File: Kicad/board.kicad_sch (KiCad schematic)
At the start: 32 parts, among them SW1 SW_Push, SW10 SW_Push, SW11 SW_Push, SW12 SW_Push, SW13 RotaryEncoder, SW2 SW_Push, SW3 SW_Push, SW4 SW_Push, SW5 SW_Push, SW6 SW_Push, SW7 SW_Push, SW8 SW_Push, SW9 SW_Push, U1 XIAO-ESP32-S3-DIP, U2 KY-023, U3 KY-023

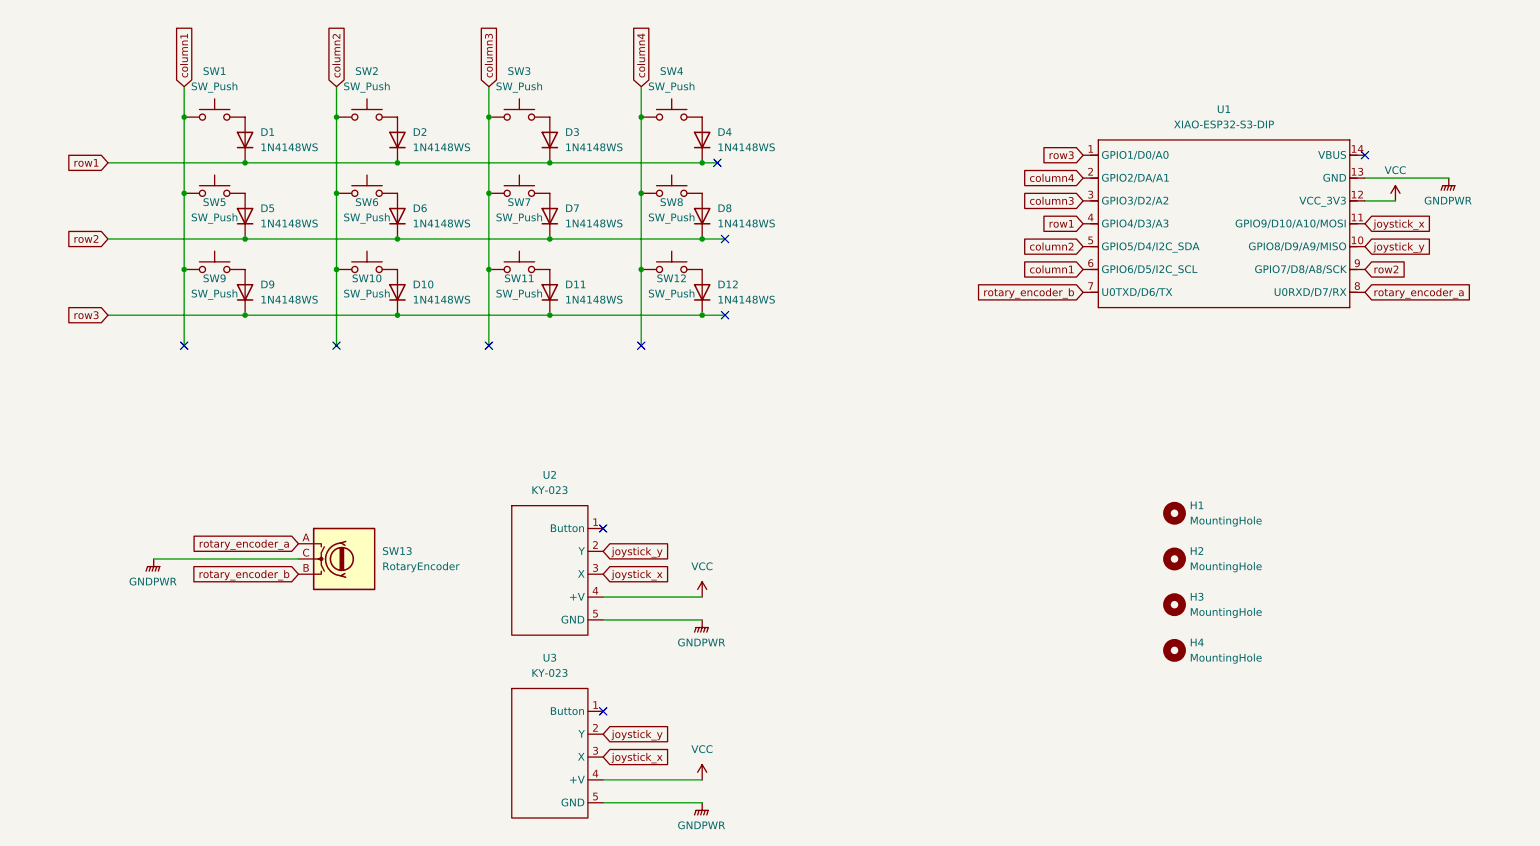
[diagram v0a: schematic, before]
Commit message: [add] add an oled device and revise pin assign
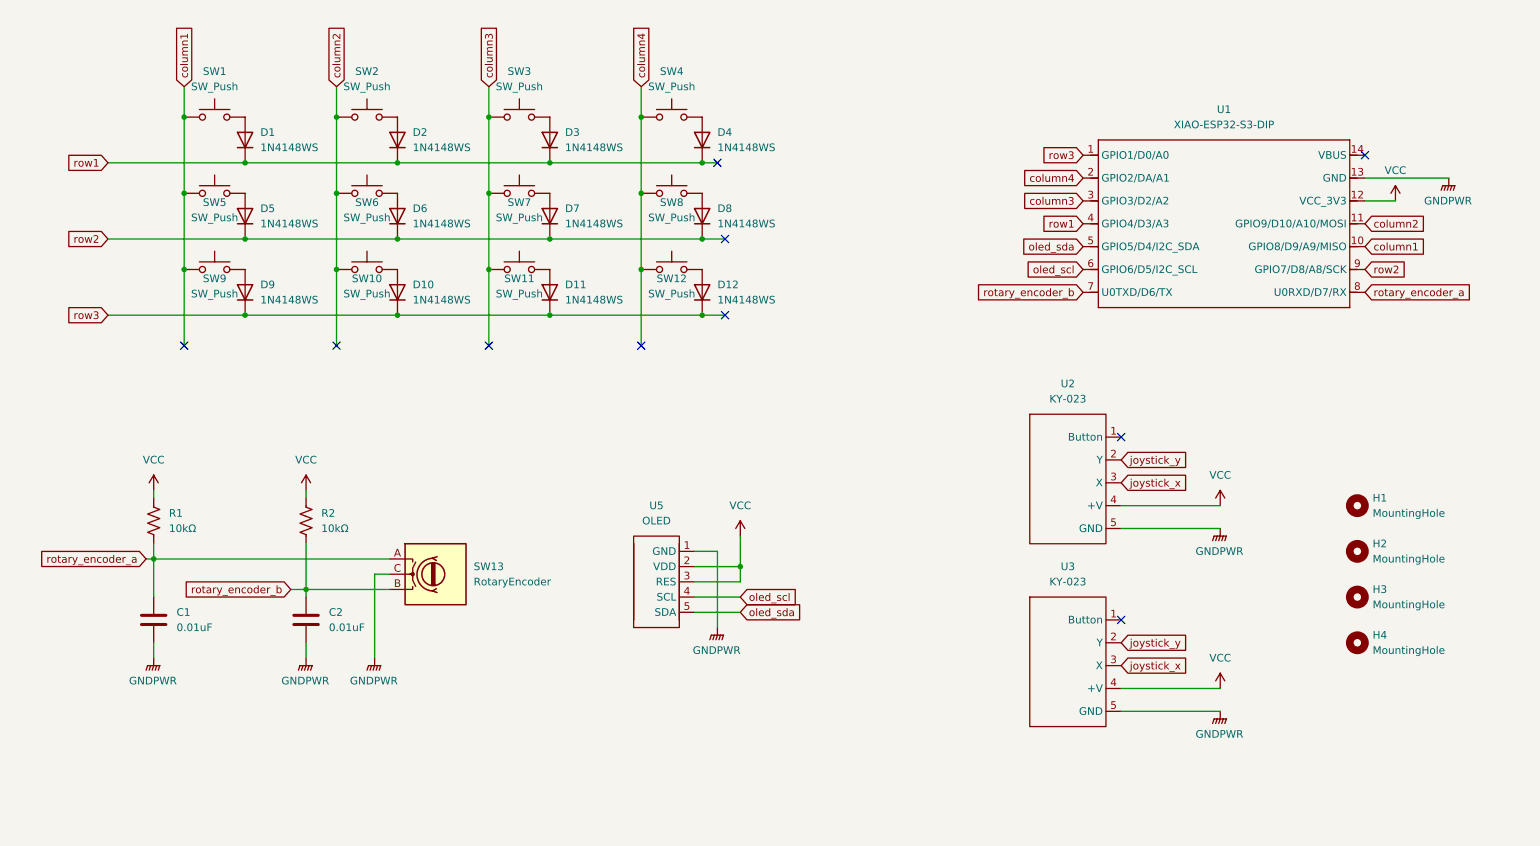
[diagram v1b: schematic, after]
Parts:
- added C1, C2: 0.01uF, symbol Device:C
- added R1, R2: 10kΩ, symbol Device:R_US
- added U5: OLED, symbol my_parts:oled
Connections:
- net GNDPWR: now also C1.2, C2.2, U5.1 (GND)
- net VCC: now also R1.1, R2.1, U5.2 (VDD), U5.3 (RES)
- net column1: now also U1.10 (GPIO8/D9/A9/MISO); no longer U1.6 (GPIO6/D5/I2C_SCL)
- net column2: now also U1.11 (GPIO9/D10/A10/MOSI); no longer U1.5 (GPIO5/D4/I2C_SDA)
- net joystick_x: no longer U1.11 (GPIO9/D10/A10/MOSI)
- net joystick_y: no longer U1.10 (GPIO8/D9/A9/MISO)
- net rotary_encoder_a: now also C1.1, R1.2
- net rotary_encoder_b: now also C2.1, R2.2
- new net oled_scl: U1.6 (GPIO6/D5/I2C_SCL), U5.4 (SCL)
- new net oled_sda: U1.5 (GPIO5/D4/I2C_SDA), U5.5 (SDA)
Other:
- moved on the sheet: H1, H2, H3, H4, SW13, U2, U3

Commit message: [update] update footprint
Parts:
- C1, C2: footprint (none) -> Capacitor_SMD:C_0805_2012Metric_Pad1.18x1.45mm_HandSolder
- D1, D10, D11, D12, D2, D3, D4, D5, D6, D7, D8, D9: value 1N4148WS -> 1N4148W; footprint mylib:1n4148ws_reversible -> Diode_THT:D_DO-35_SOD27_P7.62mm_Horizontal
- R1, R2: footprint (none) -> Resistor_THT:R_Axial_DIN0207_L6.3mm_D2.5mm_P10.16mm_Horizontal
- U2: now left out of the parts list
- U4: renamed from U3; now left out of the parts list
- renumbered U5 to U3
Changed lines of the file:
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@@
 			)
 		)
-		(property "Footprint" ""
+		(property "Footprint" "Resistor_THT:R_Axial_DIN0207_L6.3mm_D2.5mm_P10.16mm_Horizontal"
 			(at 68.326 118.364 90)
 			(effects
@@
 		(unit 1)
 		(exclude_from_sim no)
-		(in_bom yes)
-		(on_board yes)
+		(in_bom no)
+		(on_board no)
 		(dnp no)
 		(fields_autoplaced yes)
-		(property "Reference" "U3"
+		(property "Reference" "U4"
 			(at 194.31 125.73 0)
 			(effects
@@
 			(project "board"
 				(path "/e49ea350-db18-4e55-8e96-c45c407ec11d"
-					(reference "U3")
+					(reference "U4")
 					(unit 1)
 				)
@@
 			)
 		)
-		(property "Value" "1N4148WS"
+		(property "Value" "1N4148W"
 			(at 110.49 55.8799 90)
 			(effects
@@
 			)
 		)
-		(property "Footprint" "mylib:1n4148ws_reversible"
+		(property "Footprint" "Diode_THT:D_DO-35_SOD27_P7.62mm_Horizontal"
 			(at 112.395 54.61 0)
 			(effects
@@
 			)
 		)
-		(property "Value" "1N4148WS"
+		(property "Value" "1N4148W"
 			(at 135.89 55.8799 90)
 			(effects
@@
 			)
 		)
-		(property "Footprint" "mylib:1n4148ws_reversible"
+		(property "Footprint" "Diode_THT:D_DO-35_SOD27_P7.62mm_Horizontal"
 			(at 137.795 54.61 0)
 			(effects
@@
 		(dnp no)
 		(fields_autoplaced yes)
-		(property "Reference" "U5"
+		(property "Reference" "U3"
 			(at 125.73 115.57 0)
 			(effects
@@
 			(project ""
 				(path "/e49ea350-db18-4e55-8e96-c45c407ec11d"
-					(reference "U5")
+					(reference "U3")
 					(unit 1)
 				)
@@
 			)
 		)
-		(property "Value" "1N4148WS"
+		(property "Value" "1N4148W"
 			(at 135.89 81.2799 90)
 			(effects
@@
 			)
 		)
-		(property "Footprint" "mylib:1n4148ws_reversible"
+		(property "Footprint" "Diode_THT:D_DO-35_SOD27_P7.62mm_Horizontal"
 			(at 137.795 80.01 0)
 			(effects
@@
 			)
 		)
-		(property "Footprint" ""
+		(property "Footprint" "Capacitor_SMD:C_0805_2012Metric_Pad1.18x1.45mm_HandSolder"
 			(at 42.8752 138.43 0)
 			(effects
@@
 		(dnp no)
 		(fields_autoplaced yes)
-		(property "Reference" "#PWR07"
+		(property "Reference" "#PWR013"
 			(at 219.71 154.94 0)
 			(effects
@@
 			(project "board"
 				(path "/e49ea350-db18-4e55-8e96-c45c407ec11d"
-					(reference "#PWR07")
+					(reference "#PWR013")
 					(unit 1)
 				)
@@
 			)
 		)
-		(property "Value" "1N4148WS"
+		(property "Value" "1N4148W"
 			(at 85.09 68.5799 90)
 			(effects
@@
 			)
 		)
-		(property "Footprint" "mylib:1n4148ws_reversible"
+		(property "Footprint" "Diode_THT:D_DO-35_SOD27_P7.62mm_Horizontal"
 			(at 86.995 67.31 0)
 			(effects
@@
 			)
 		)
-		(property "Value" "1N4148WS"
+		(property "Value" "1N4148W"
 			(at 59.69 81.2799 90)
 			(effects
@@
 			)
 		)
-		(property "Footprint" "mylib:1n4148ws_reversible"
+		(property "Footprint" "Diode_THT:D_DO-35_SOD27_P7.62mm_Horizontal"
 			(at 61.595 80.01 0)
 			(effects
@@
 		(unit 1)
 		(exclude_from_sim no)
-		(in_bom yes)
-		(on_board yes)
+		(in_bom no)
+		(on_board no)
 		(dnp no)
 		(fields_autoplaced yes)
@@
 		(dnp no)
 		(fields_autoplaced yes)
-		(property "Reference" "#PWR012"
+		(property "Reference" "#PWR07"
 			(at 139.7 124.46 0)
 			(effects
@@
 			(project ""
 				(path "/e49ea350-db18-4e55-8e96-c45c407ec11d"
-					(reference "#PWR012")
+					(reference "#PWR07")
 					(unit 1)
 				)
@@
 			)
 		)
-		(property "Value" "1N4148WS"
+		(property "Value" "1N4148W"
 			(at 85.09 81.2799 90)
 			(effects
@@
 			)
 		)
-		(property "Footprint" "mylib:1n4148ws_reversible"
+		(property "Footprint" "Diode_THT:D_DO-35_SOD27_P7.62mm_Horizontal"
 			(at 86.995 80.01 0)
 			(effects
@@
 		(dnp no)
 		(fields_autoplaced yes)
-		(property "Reference" "#PWR06"
+		(property "Reference" "#PWR012"
 			(at 219.71 149.86 0)
 			(effects
@@
 			(project "board"
 				(path "/e49ea350-db18-4e55-8e96-c45c407ec11d"
-					(reference "#PWR06")
+					(reference "#PWR012")
 					(unit 1)
 				)
@@
 		(dnp no)
 		(fields_autoplaced yes)
-		(property "Reference" "#PWR09"
+		(property "Reference" "#PWR04"
 			(at 67.31 116.84 0)
 			(effects
@@
 			(project "board"
 				(path "/e49ea350-db18-4e55-8e96-c45c407ec11d"
-					(reference "#PWR09")
+					(reference "#PWR04")
 					(unit 1)
 				)
@@
 			)
 		)
-		(property "Value" "1N4148WS"
+		(property "Value" "1N4148W"
 			(at 135.89 68.5799 90)
 			(effects
@@
 			)
 		)
-		(property "Footprint" "mylib:1n4148ws_reversible"
+		(property "Footprint" "Diode_THT:D_DO-35_SOD27_P7.62mm_Horizontal"
 			(at 137.795 67.31 0)
 			(effects
@@
 			)
 		)
-		(property "Value" "1N4148WS"
+		(property "Value" "1N4148W"
 			(at 110.49 81.2799 90)
 			(effects
@@
 			)
 		)
-		(property "Footprint" "mylib:1n4148ws_reversible"
+		(property "Footprint" "Diode_THT:D_DO-35_SOD27_P7.62mm_Horizontal"
 			(at 112.395 80.01 0)
 			(effects
@@
 		(dnp no)
 		(fields_autoplaced yes)
-		(property "Reference" "#PWR013"
+		(property "Reference" "#PWR08"
 			(at 135.89 140.97 0)
 			(effects
@@
 			(project ""
 				(path "/e49ea350-db18-4e55-8e96-c45c407ec11d"
-					(reference "#PWR013")
+					(reference "#PWR08")
 					(unit 1)
 				)
@@
 		(dnp no)
 		(fields_autoplaced yes)
-		(property "Reference" "#PWR05"
+		(property "Reference" "#PWR06"
 			(at 219.71 124.46 0)
 			(effects
@@
 			(project ""
 				(path "/e49ea350-db18-4e55-8e96-c45c407ec11d"
-					(reference "#PWR05")
+					(reference "#PWR06")
 					(unit 1)
 				)
@@
 			)
 		)
-		(property "Footprint" ""
+		(property "Footprint" "Capacitor_SMD:C_0805_2012Metric_Pad1.18x1.45mm_HandSolder"
 			(at 68.2752 138.43 0)
 			(effects
@@
 			)
 		)
-		(property "Value" "1N4148WS"
+		(property "Value" "1N4148W"
 			(at 59.69 68.5799 90)
 			(effects
@@
 			)
 		)
-		(property "Footprint" "mylib:1n4148ws_reversible"
+		(property "Footprint" "Diode_THT:D_DO-35_SOD27_P7.62mm_Horizontal"
 			(at 61.595 67.31 0)
 			(effects
@@
 		(dnp no)
 		(fields_autoplaced yes)
-		(property "Reference" "#PWR011"
+		(property "Reference" "#PWR010"
 			(at 67.31 146.05 0)
 			(effects
@@
 			(project "board"
 				(path "/e49ea350-db18-4e55-8e96-c45c407ec11d"
-					(reference "#PWR011")
+					(reference "#PWR010")
 					(unit 1)
 				)
@@
 		(dnp no)
 		(fields_autoplaced yes)
-		(property "Reference" "#PWR03"
+		(property "Reference" "#PWR011"
 			(at 78.74 146.05 0)
 			(effects
@@
 			(project ""
 				(path "/e49ea350-db18-4e55-8e96-c45c407ec11d"
-					(reference "#PWR03")
+					(reference "#PWR011")
 					(unit 1)
 				)
@@
 		(dnp no)
 		(fields_autoplaced yes)
-		(property "Reference" "#PWR04"
+		(property "Reference" "#PWR05"
 			(at 219.71 119.38 0)
 			(effects
@@
 			(project ""
 				(path "/e49ea350-db18-4e55-8e96-c45c407ec11d"
-					(reference "#PWR04")
+					(reference "#PWR05")
 					(unit 1)
 				)
@@
 			)
 		)
-		(property "Value" "1N4148WS"
+		(property "Value" "1N4148W"
 			(at 85.09 55.8799 90)
 			(effects
@@
 			)
 		)
-		(property "Footprint" "mylib:1n4148ws_reversible"
+		(property "Footprint" "Diode_THT:D_DO-35_SOD27_P7.62mm_Horizontal"
 			(at 86.995 54.61 0)
 			(effects
@@
 			)
 		)
-		(property "Footprint" ""
+		(property "Footprint" "Resistor_THT:R_Axial_DIN0207_L6.3mm_D2.5mm_P10.16mm_Horizontal"
 			(at 42.926 118.364 90)
 			(effects
@@
 			)
 		)
-		(property "Value" "1N4148WS"
+		(property "Value" "1N4148W"
 			(at 110.49 68.5799 90)
 			(effects
@@
 			)
 		)
-		(property "Footprint" "mylib:1n4148ws_reversible"
+		(property "Footprint" "Diode_THT:D_DO-35_SOD27_P7.62mm_Horizontal"
 			(at 112.395 67.31 0)
 			(effects
@@
 			)
 		)
-		(property "Value" "1N4148WS"
+		(property "Value" "1N4148W"
 			(at 59.69 55.8799 90)
 			(effects
@@
 			)
 		)
-		(property "Footprint" "mylib:1n4148ws_reversible"
+		(property "Footprint" "Diode_THT:D_DO-35_SOD27_P7.62mm_Horizontal"
 			(at 61.595 54.61 0)
 			(effects
@@
 		(dnp no)
 		(fields_autoplaced yes)
-		(property "Reference" "#PWR010"
+		(property "Reference" "#PWR09"
 			(at 41.91 146.05 0)
 			(effects
@@
 			(project "board"
 				(path "/e49ea350-db18-4e55-8e96-c45c407ec11d"
-					(reference "#PWR010")
+					(reference "#PWR09")
 					(unit 1)
 				)
@@
 		(dnp no)
 		(fields_autoplaced yes)
-		(property "Reference" "#PWR08"
+		(property "Reference" "#PWR03"
 			(at 41.91 116.84 0)
 			(effects
@@
 			(project ""
 				(path "/e49ea350-db18-4e55-8e96-c45c407ec11d"
-					(reference "#PWR08")
+					(reference "#PWR03")
 					(unit 1)
 				)

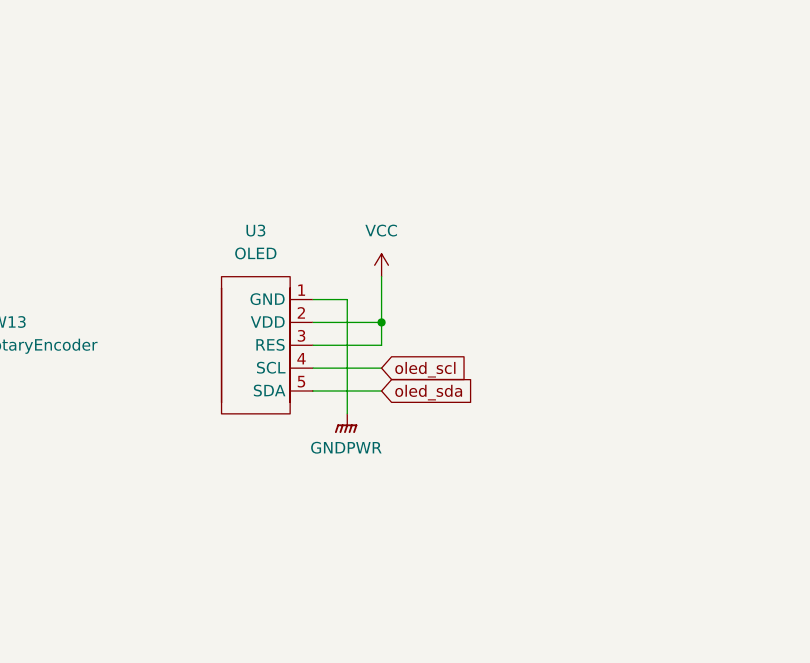
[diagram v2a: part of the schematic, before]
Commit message: [add] add solder jumpers to support reversible pin holes
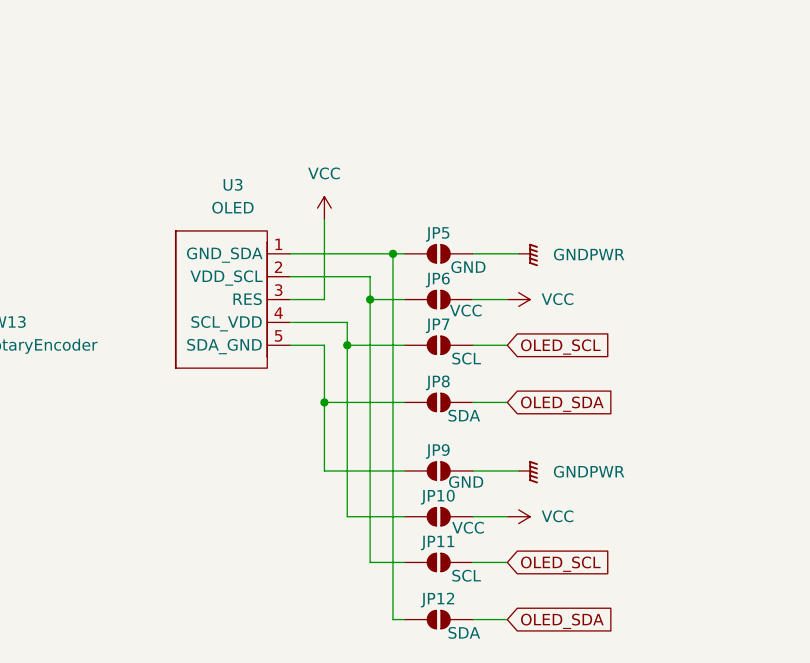
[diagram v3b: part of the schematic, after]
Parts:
- added JP10, JP6: VCC, Jumper:SolderJumper-2_P1.3mm_Open_TrianglePad1.0x1.5mm, symbol Jumper:SolderJumper_2_Open
- added JP11, JP7: SCL, Jumper:SolderJumper-2_P1.3mm_Open_TrianglePad1.0x1.5mm, symbol Jumper:SolderJumper_2_Open
- added JP12, JP8: SDA, Jumper:SolderJumper-2_P1.3mm_Open_TrianglePad1.0x1.5mm, symbol Jumper:SolderJumper_2_Open
- added JP5, JP9: GND, Jumper:SolderJumper-2_P1.3mm_Open_TrianglePad1.0x1.5mm, symbol Jumper:SolderJumper_2_Open
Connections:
- net GNDPWR: now also JP5.2 (B), JP9.2 (B); no longer U3.1 (GND)
- net VCC: now also JP10.2 (B), JP6.2 (B); no longer U3.2 (VDD)
- net oled_scl: no longer U3.4 (SCL)
- net oled_sda: no longer U3.5 (SDA)
- new net: JP12.1 (A), JP5.1 (A), U3.1 (GND_SDA)
- new net: JP11.1 (A), JP6.1 (A), U3.2 (VDD_SCL)
- new net: JP10.1 (A), JP7.1 (A), U3.4 (SCL_VDD)
- new net: JP8.1 (A), JP9.1 (A), U3.5 (SDA_GND)
- new net OLED_SCL: JP11.2 (B), JP7.2 (B)
- new net OLED_SDA: JP12.2 (B), JP8.2 (B)
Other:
- moved on the sheet: U3
